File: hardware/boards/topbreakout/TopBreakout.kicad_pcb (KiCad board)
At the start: 2 copper layers, 75.6 x 73 mm, 46 parts, among them J1 WURTH_ELECTRONICS_61400413321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, J2 MOLEX_52892-3033MOLEX_52892-3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, J3 USB-A-S-X-X-VT, U1 ANALOG_DEVICES_AD7606BSTZANAL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, U3 ANALOG_DEVICES_AD5754BREZANAL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, U5 MICROCHIP_MCP1700T-2502E-TTMI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

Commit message: cleanup
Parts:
- removed MIDI_IN, MIDI_OUT: OG-MIDI_MAB5SHCUI-SD-50BV, OG-MIDI_SD-50BV
- added MIDI_IN1: OG-MIDI_MAB5SHCUI-SD-50BV, topbreakout:OG-MIDI_SD-50BV, F.Cu at (117.7, 91.4)
- added MIDI_OUT1: OG-MIDI_MAB5SHCUI-SD-50BV, topbreakout:OG-MIDI_SD-50BV, F.Cu at (178.7, 91.3)
- C1, C2, C3, C4: footprint C0805K -> topbreakout:C0805K
- C10, C11, C6, C9: footprint C1206 -> topbreakout:C1206
- C5, C7, C8: footprint 1206 -> topbreakout:1206
- J1: footprint WURTH_ELECTRONICS_61400413321_0 -> topbreakout:WURTH_ELECTRONICS_61400413321_0
- J2: value MOLEX_52892-3033MOLEX_52892-3033_0_0 -> MOLEX_52892-3033; footprint MOLEX_52892-3033_0 -> topbreakout:MOLEX_52892-3033_0
- J3: footprint USB-A-S-X-X-VT -> topbreakout:USB-A-S-X-X-VT
- J4: value (none) -> ST7735_1.4; footprint ST7735 -> topbreakout:ST7735
- JAD1, JAD2, JAD3, JAD4, JAD5, JAD6, JAD7, JAD8, JDA1, JDA2, JDA3, JDA4, JDA5, JDA6, JDA7, JDA8: footprint WQP-PJ301M-12_JACK -> topbreakout:WQP-PJ301M-12_JACK
- R10, R4, R7, R8, R9: footprint R0805 -> Capacitors_SMD:C_0805
- R11: footprint R0805 -> topbreakout:R0805
- TP1, TP3: footprint PAD.03X.05 -> topbreakout:PAD.03X.05
- U$1: footprint YAMAICHI_MICROSD_VERTICAL -> topbreakout:YAMAICHI_MICROSD_VERTICAL
- U$2: footprint TE_1-1734592-8 -> topbreakout:TE_1-1734592-8
- U1: footprint ANALOG_DEVICES_AD7606BSTZ_2 -> topbreakout:ANALOG_DEVICES_AD7606BSTZ_2
- U3: footprint ANALOG_DEVICES_AD5754BREZ_2 -> topbreakout:ANALOG_DEVICES_AD5754BREZ_2
- U5: value MICROCHIP_MCP1700T-2502E-TTMICROCHIP_MCP1700T-2502E-TT_0_0 -> MCP1700T-2502E; footprint MICROCHIP_MCP1700T-2502E-TT_0 -> topbreakout:MICROCHIP_MCP1700T-2502E-TT_0
- moved U5 27.1 mm to (117.3, 114.3), turned to 180 degrees
- moved C9 15.0 mm to (122.7, 114.3), turned to 0 degrees
- moved C6 14.9 mm to (128.8, 114.3), turned to 180 degrees
- moved C10 12.8 mm to (140.7, 138.3), turned to 270 degrees
- moved TP1 9.25 mm to (166.9, 136.4)
- moved R10 7.66 mm to (162.1, 139.8), turned to 180 degrees
- moved R4 6.29 mm to (157.6, 139.1), turned to 180 degrees
- moved C11 6.02 mm to (144.3, 138.3)
- moved U3 5.94 mm to (123.8, 121.9), turned to 0 degrees
- moved R9 5.33 mm to (153.3, 140.0), turned to 0 degrees
- moved TP3 5.31 mm to (119.1, 116.8)
- moved R8 4.04 mm to (148.7, 140.0), turned to 180 degrees
- moved C2 3.86 mm to (169.8, 136.4)
- moved C1 3.86 mm to (169.8, 133.9)
- moved C3 3.86 mm to (169.8, 131.4)
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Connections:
- net AD_AGND renamed /io_breakout-ver2.1_5/AD_AGND
- net AD_BYTE_SELECT renamed /io_breakout-ver2.1_5/AD_BYTE_SELECT
- net AD_OS0 renamed /io_breakout-ver2.1_5/AD_OS0
- net AD_RANGE renamed /io_breakout-ver2.1_5/AD_RANGE
- net AD_REFCAP_A renamed /io_breakout-ver2.1_5/AD_REFCAP_A
- net AD_REFSEL renamed /io_breakout-ver2.1_5/AD_REFSEL
- net AD_REGCAP1 renamed /io_breakout-ver2.1_5/AD_REGCAP1
- net AD_REGCAP2 renamed /io_breakout-ver2.1_5/AD_REGCAP2
- net AD_STBY renamed /io_breakout-ver2.1_5/AD_STBY
- net AGND renamed /io_breakout-ver2.1_5/AGND
- net AVIN renamed /io_breakout-ver2.1_5/AVIN
- net SD_CLK renamed /io_breakout-ver2.1_3/SD_CLK
- net SD_CS renamed /io_breakout-ver2.1_3/SD_CS
- net SD_DAT1 renamed /io_breakout-ver2.1_3/SD_DAT1
- net SD_DAT2 renamed /io_breakout-ver2.1_3/SD_DAT2
- net SD_DATAIN renamed /io_breakout-ver2.1_3/SD_DATAIN
- net SD_DATAOUT renamed /io_breakout-ver2.1_3/SD_DATAOUT
- net SD_GND renamed /io_breakout-ver2.1_3/SD_GND
- net SD_VCC renamed /io_breakout-ver2.1_3/SD_VCC
- net USB_A_D+ renamed /io_breakout-ver2.1_3/USB_A_D+
- net USB_A_D- renamed /io_breakout-ver2.1_3/USB_A_D-
- net USB_A_VCC renamed /io_breakout-ver2.1_3/USB_A_VCC
- net USB_B_D+ renamed /io_breakout-ver2.1_3/USB_B_D+
- net USB_B_D- renamed /io_breakout-ver2.1_3/USB_B_D-
- net USB_B_VCC renamed /io_breakout-ver2.1_3/USB_B_VCC
- net VREF renamed /io_breakout-ver2.1_6/VREF
- J2 pad 10: (no net) -> AVSS
- J2 pad 12: (no net) -> AVDD
- J2 pad 13: (no net) -> AVDD
- J2 pad 15: MIDI_IN_PIN5 -> /io_breakout-ver2.1_3/MIDI_IN_PIN5
- J2 pad 16: MIDI_IN_PIN4 -> /io_breakout-ver2.1_3/MIDI_IN_PIN4
- J2 pad 17: MIDI_OUT_PIN5 -> /io_breakout-ver2.1_3/MIDI_OUT_PIN5
- J2 pad 18: MIDI_OUT_PIN4 -> /io_breakout-ver2.1_3/MIDI_OUT_PIN4
- J2 pad 8: N$6 -> (no net)
- J2 pad 9: (no net) -> AVSS
- JDA5 pad P$1_TIP: DA_V5 -> (no net)
- JDA6 pad P$1_TIP: DA_V6 -> (no net)
- U1 pad 42: AD_REFINOUT -> (no net)
- U1 pad 57: AD_V5 -> (no net)
- U1 pad 59: AD_V6 -> (no net)
- U1 pad 61: AD_V7 -> (no net)
- U1 pad 63: AD_V8 -> (no net)
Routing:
- net /io_breakout-ver2.1_3/MIDI_OUT_PIN4: track 0.00 -> 84.7 mm, vias 0 -> 1
- net /io_breakout-ver2.1_3/MIDI_OUT_PIN5: track 0.00 -> 80.1 mm, vias 0 -> 1
- net MIDI_OUT_PIN4: track 75.0 -> 0.00 mm, vias 1 -> 0
- net MIDI_OUT_PIN5: track 74.2 -> 0.00 mm, vias 1 -> 0
- net /io_breakout-ver2.1_3/MIDI_IN_PIN4: track 0.00 -> 62.2 mm, vias 0 -> 1
- net MIDI_IN_PIN5: track 57.2 -> 0.00 mm
- net /io_breakout-ver2.1_3/MIDI_IN_PIN5: track 0.00 -> 48.2 mm, vias 0 -> 1
- net SPI0_MISO: track 89.0 -> 41.8 mm, vias 0 -> 3
- net MIDI_IN_PIN4: track 47.0 -> 0.00 mm
- net GND: track 5.42 -> 50.9 mm, vias 2 -> 45
- net /io_breakout-ver2.1_5/AD_AGND: track 81.3 -> 48.7 mm, vias 2 -> 1
- net /io_breakout-ver2.1_3/USB_B_D+: track 60.0 -> 91.1 mm, vias 1 -> 2
- net VIN: track 73.3 -> 102.7 mm
- net AVSS: track 0.00 -> 17.9 mm, vias 0 -> 2
- net /io_breakout-ver2.1_5/AD_REFSEL: track 11.5 -> 27.4 mm
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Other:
- rule trace_min: 0.2 -> 0.12
- rule via_min_drill: 0.3 -> 0.25

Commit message: minor
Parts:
- added J5: Conn_01x40, Connectors_TE-Connectivity:TE_2-84953-7_1x27_P1.0mm_Horizontal, F.Cu at (226.8, 98.8)
- J2: value MOLEX_52892-3033 -> MOLEX_52892-3033MOLEX_52892-3033_0_0
- R10, R4, R7, R8, R9: footprint Capacitors_SMD:C_0805 -> Resistors_SMD:R_0805
- R11: footprint topbreakout:R0805 -> Oddities:NetTie-I_Connected_SMD
- U5: value MCP1700T-2502E -> MICROCHIP_MCP1700T-2502E-TTMICROCHIP_MCP1700T-2502E-TT_0_0
- moved R4 1.69 mm to (157.2, 140.7), turned to 90 degrees
- moved R10 1.02 mm to (161.5, 140.7), turned to 90 degrees
- moved R9 1.01 mm to (153.9, 140.7), turned to 270 degrees
- moved R8 0.77 mm to (148.6, 140.7), turned to 90 degrees
- moved R11 0.17 mm to (155.8, 128.7), turned to 90 degrees
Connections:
- net /io_breakout-ver2.1_3/MIDI_IN_PIN4 renamed /FPC connector/MIDI_IN_PIN4
- net /io_breakout-ver2.1_3/MIDI_IN_PIN5 renamed /FPC connector/MIDI_IN_PIN5
- net /io_breakout-ver2.1_3/MIDI_OUT_PIN4 renamed /FPC connector/MIDI_OUT_PIN4
- net /io_breakout-ver2.1_3/MIDI_OUT_PIN5 renamed /FPC connector/MIDI_OUT_PIN5
- net /io_breakout-ver2.1_3/SD_CLK renamed /FPC connector/SD_CLK
- net /io_breakout-ver2.1_3/SD_CS renamed /FPC connector/SD_CS
- net /io_breakout-ver2.1_3/SD_DAT1 renamed /FPC connector/SD_DAT1
- net /io_breakout-ver2.1_3/SD_DAT2 renamed /FPC connector/SD_DAT2
- net /io_breakout-ver2.1_3/SD_DATAIN renamed /FPC connector/SD_DATAIN
- net /io_breakout-ver2.1_3/SD_DATAOUT renamed /FPC connector/SD_DATAOUT
- net /io_breakout-ver2.1_3/SD_GND renamed /FPC connector/SD_GND
- net /io_breakout-ver2.1_3/SD_VCC renamed /FPC connector/SD_VCC
- net /io_breakout-ver2.1_3/USB_A_D+ renamed /FPC connector/USB_A_D+
- net /io_breakout-ver2.1_3/USB_A_D- renamed /FPC connector/USB_A_D-
- net /io_breakout-ver2.1_3/USB_A_VCC renamed /FPC connector/USB_A_VCC
- net /io_breakout-ver2.1_3/USB_B_D+ renamed /FPC connector/USB_B_D+
- net /io_breakout-ver2.1_3/USB_B_D- renamed /FPC connector/USB_B_D-
- net /io_breakout-ver2.1_3/USB_B_VCC renamed /FPC connector/USB_B_VCC
- net /io_breakout-ver2.1_5/AD_AGND renamed /AD7606/AD_AGND
- net /io_breakout-ver2.1_5/AD_BYTE_SELECT renamed /AD7606/AD_BYTE_SELECT
- net /io_breakout-ver2.1_5/AD_OS0 renamed /AD7606/AD_OS0
- net /io_breakout-ver2.1_5/AD_RANGE renamed /AD7606/AD_RANGE
- net /io_breakout-ver2.1_5/AD_REFCAP_A renamed /AD7606/AD_REFCAP_A
- net /io_breakout-ver2.1_5/AD_REFSEL renamed /AD7606/AD_REFSEL
- net /io_breakout-ver2.1_5/AD_REGCAP1 renamed /AD7606/AD_REGCAP1
- net /io_breakout-ver2.1_5/AD_REGCAP2 renamed /AD7606/AD_REGCAP2
- net /io_breakout-ver2.1_5/AD_STBY renamed /AD7606/AD_STBY
- net /io_breakout-ver2.1_5/AGND renamed /AD7606/AGND
- net /io_breakout-ver2.1_5/AVIN renamed /AD7606/AVIN
- net /io_breakout-ver2.1_6/VREF renamed /AD5754 DAC/VREF
- JAD5 pad P$2_SWITCH: TAGND -> Net-(JAD5-PadP$2_SWITCH)
- JAD5 pad P$3_SLEEVE: TAGND -> Net-(JAD5-PadP$2_SWITCH)
- JAD6 pad P$2_SWITCH: TAGND -> Net-(JAD6-PadP$2_SWITCH)
- JAD6 pad P$3_SLEEVE: TAGND -> Net-(JAD6-PadP$2_SWITCH)
- JDA5 pad P$3_SLEEVE: TAGND -> GND
- JDA6 pad P$3_SLEEVE: TAGND -> GND
- JDA7 pad P$3_SLEEVE: (no net) -> GND
- JDA8 pad P$3_SLEEVE: (no net) -> GND
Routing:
- net GND: track 50.9 -> 73.7 mm, vias 45 -> 46
- net /AD7606/AD_AGND: track 48.7 -> 54.8 mm, vias 1 -> 4
- net 3V3: track 107.5 -> 111.5 mm, vias 3 -> 4
- net /FPC connector/USB_B_VCC: track 86.5 -> 88.4 mm
- net /AD7606/AD_STBY: track 7.45 -> 6.39 mm
- net /AD7606/AD_RANGE: track 11.1 -> 10.3 mm
- net /AD7606/AD_BYTE_SELECT: track 4.83 -> 5.37 mm

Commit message: moved midi circuit to breakout board
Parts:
- removed J5: Conn_01x40, Connectors_TE-Connectivity:TE_2-84953-7_1x27_P1.0mm_Horizontal
- added D1: D, Diodes_SMD:D_0805, B.Cu at (129.8, 92.6)
- added R1: 220, Resistors_SMD:R_0805_HandSoldering, B.Cu at (129.8, 83.6)
- added R2: 220, Resistors_SMD:R_0805_HandSoldering, B.Cu at (130.0, 97.0)
- added R3: 220, Resistors_SMD:R_0805_HandSoldering, B.Cu at (162.8, 90.9)
- added R5: 220, Resistors_SMD:R_0805_HandSoldering, B.Cu at (129.8, 88.1)
- added U$3: OPTO_DARL_6N138S, Mainboard:8-SMD, B.Cu at (145.8, 91.2)
- moved R10 2.70 mm to (163.6, 138.9)
- moved R4 2.29 mm to (158.7, 138.9)
- moved R8 1.80 mm to (148.8, 138.9)
- moved R9 1.79 mm to (153.8, 138.9)
- moved C3 1.56 mm to (169.8, 129.8)
- moved TP1 1.44 mm to (165.9, 135.4)
- moved C1 1.04 mm to (169.8, 132.9)
- moved C2 0.52 mm to (169.8, 135.9)
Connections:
- net /FPC connector/MIDI_IN_PIN4 renamed MIDI_IN_PIN4
- net /FPC connector/MIDI_IN_PIN5 renamed MIDI_IN_PIN5
- net /FPC connector/MIDI_OUT_PIN4 renamed MIDI_OUT_PIN4
- net /FPC connector/MIDI_OUT_PIN5 renamed MIDI_OUT_PIN5
- JAD5 pad P$1_TIP: (no net) -> AD_V5
- JAD6 pad P$1_TIP: (no net) -> AD_V6
- JAD7 pad P$1_TIP: (no net) -> AD_V7
- JAD8 pad P$1_TIP: (no net) -> AD_V8
- U1 pad 57: (no net) -> AD_V5
- U1 pad 59: (no net) -> AD_V6
- U1 pad 61: (no net) -> AD_V7
- U1 pad 63: (no net) -> AD_V8
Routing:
- net 3V3: track 111.5 -> 0.00 mm, vias 4 -> 0
- net VIN: track 102.7 -> 0.00 mm, vias 1 -> 0
- net /FPC connector/USB_B_D+: track 91.1 -> 0.00 mm, vias 2 -> 0
- net /FPC connector/USB_B_VCC: track 88.4 -> 0.00 mm, vias 1 -> 0
- net MIDI_OUT_PIN4: track 84.7 -> 0.00 mm, vias 1 -> 0
- net MIDI_OUT_PIN5: track 80.1 -> 0.00 mm, vias 1 -> 0
- net GND: track 73.7 -> 0.00 mm, vias 46 -> 0
- net SPI0_SCK: track 70.9 -> 0.00 mm, vias 2 -> 0
- net /FPC connector/USB_B_D-: track 70.5 -> 0.00 mm, vias 1 -> 0
- net AD_V1: track 68.4 -> 0.00 mm, vias 1 -> 0
- net AD_V2: track 65.9 -> 0.00 mm
- net MIDI_IN_PIN4: track 62.2 -> 0.00 mm, vias 1 -> 0
- net AD_V3: track 60.8 -> 0.00 mm
- net AD_V4: track 58.2 -> 0.00 mm
- net /AD7606/AD_AGND: track 54.8 -> 0.00 mm, vias 4 -> 0
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
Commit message: refactor
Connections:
- J2 pad 10: AVSS -> AVDD
- J2 pad 11: (no net) -> AVDD
- J2 pad 12: AVDD -> GATE_4
- J2 pad 13: AVDD -> GATE_3
- J2 pad 14: (no net) -> GATE_2
- J2 pad 15: MIDI_IN_PIN5 -> GATE_1
- J2 pad 16: MIDI_IN_PIN4 -> (no net)
- J2 pad 17: MIDI_OUT_PIN5 -> MIDI_TX
- J2 pad 18: MIDI_OUT_PIN4 -> MIDI_RX
- J2 pad 8: (no net) -> AVSS
- JDA5 pad P$1_TIP: (no net) -> GATE_1
- JDA6 pad P$1_TIP: (no net) -> GATE_2
- JDA7 pad P$1_TIP: (no net) -> GATE_3
- JDA8 pad P$1_TIP: (no net) -> GATE_4
- R3 pad 2: (no net) -> MIDI_TX

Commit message: imporvements
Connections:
- JAD5 pad P$2_SWITCH: Net-(JAD5-PadP$2_SWITCH) -> GND
- JAD5 pad P$3_SLEEVE: Net-(JAD5-PadP$2_SWITCH) -> GND
- JAD6 pad P$2_SWITCH: Net-(JAD6-PadP$2_SWITCH) -> GND
- JAD6 pad P$3_SLEEVE: Net-(JAD6-PadP$2_SWITCH) -> GND
- JAD7 pad P$2_SWITCH: (no net) -> GND
- JAD7 pad P$3_SLEEVE: (no net) -> GND
- JAD8 pad P$2_SWITCH: (no net) -> GND
- JAD8 pad P$3_SLEEVE: (no net) -> GND

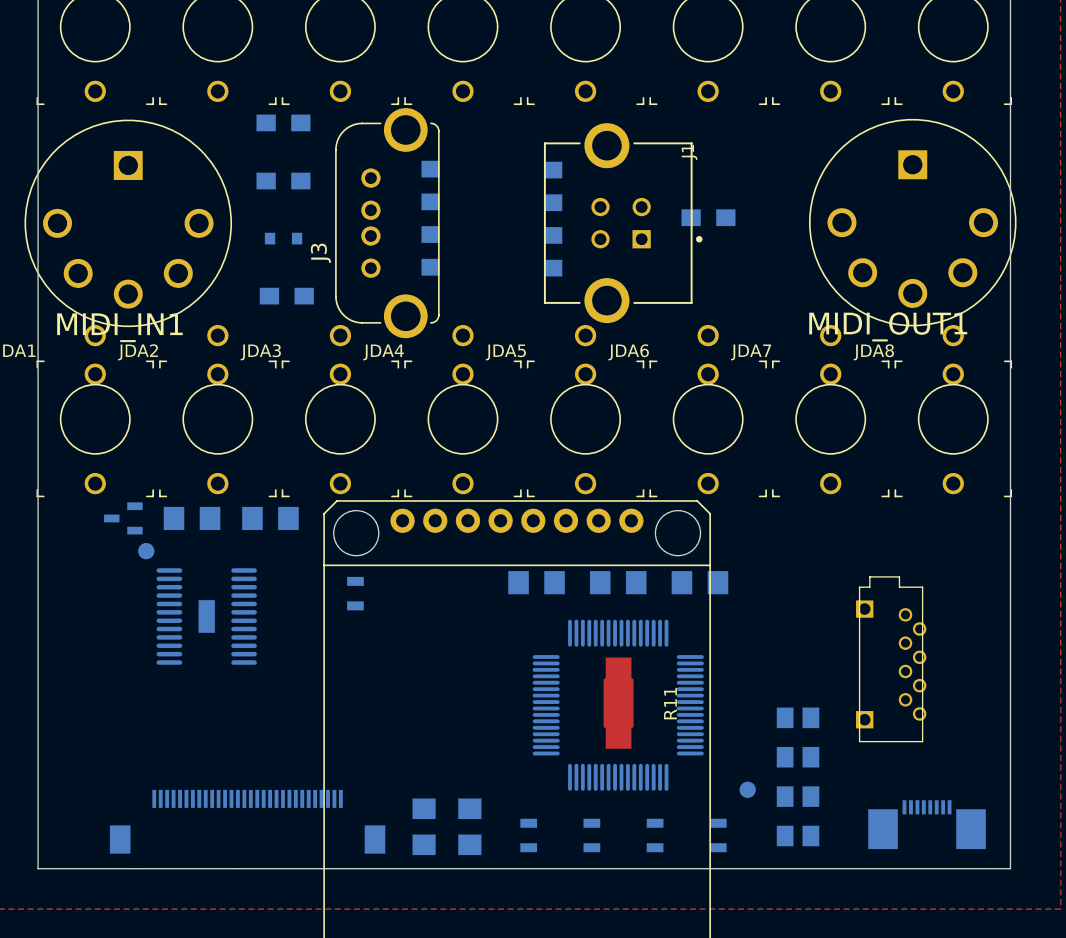
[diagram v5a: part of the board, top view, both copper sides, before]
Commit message: auto routed, not complete
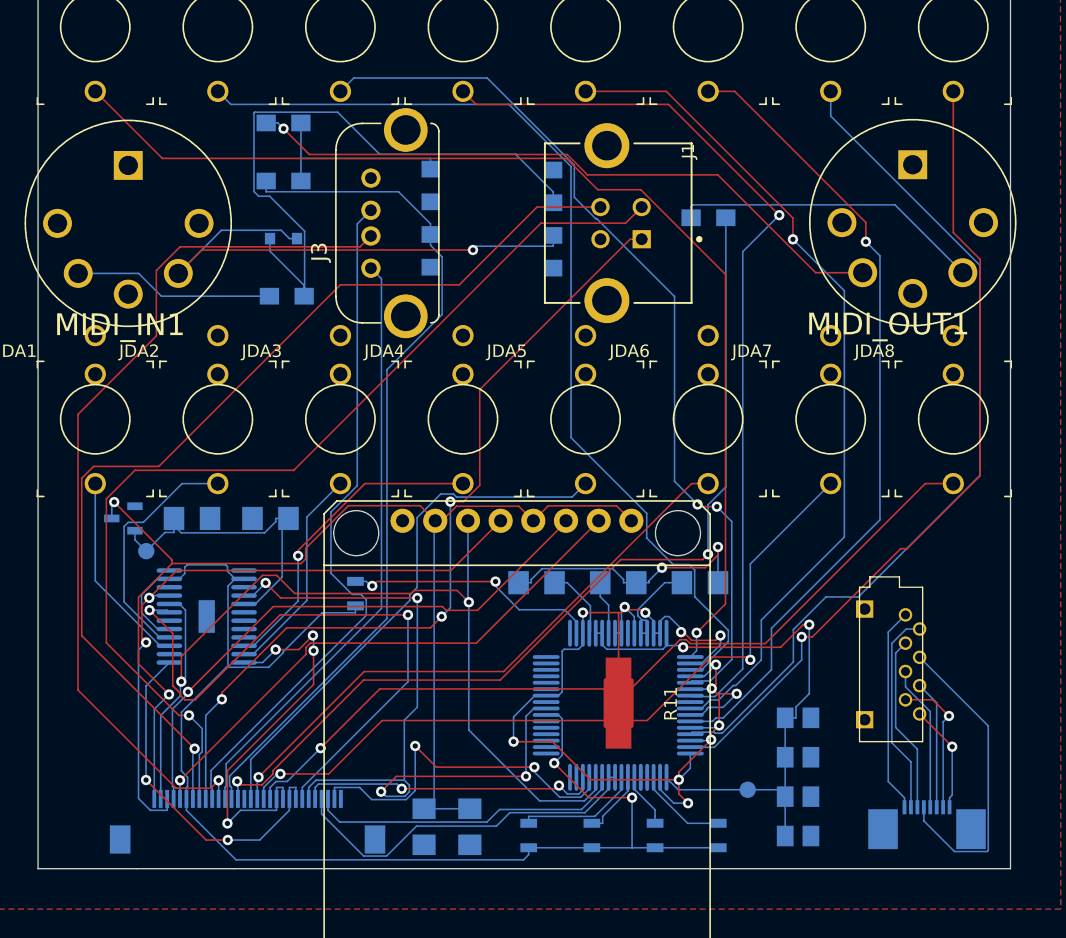
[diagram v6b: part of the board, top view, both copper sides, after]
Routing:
- net 3V3: track 0.00 -> 106.0 mm, vias 0 -> 2
- net VIN: track 0.00 -> 95.2 mm, vias 0 -> 2
- net /AD7606/AD_AGND: track 0.00 -> 88.2 mm, vias 0 -> 13
- net AD_V1: track 0.00 -> 85.7 mm, vias 0 -> 1
- net /FPC connector/USB_B_D-: track 0.00 -> 77.9 mm, vias 0 -> 1
- net /FPC connector/USB_B_D+: track 0.00 -> 77.6 mm, vias 0 -> 1
- net AD_V2: track 0.00 -> 76.5 mm
- net SPI0_SCK: track 0.00 -> 74.6 mm, vias 0 -> 2
- net MIDI_TX: track 0.00 -> 72.4 mm, vias 0 -> 2
- net AD_V4: track 0.00 -> 70.0 mm, vias 0 -> 1
- net AD_V3: track 0.00 -> 69.7 mm, vias 0 -> 2
- net /FPC connector/USB_A_D-: track 0.00 -> 68.7 mm, vias 0 -> 1
- net AD_V7: track 0.00 -> 67.0 mm
- net MIDI_RX: track 0.00 -> 66.6 mm
- net AD_V5: track 0.00 -> 65.9 mm, vias 0 -> 1
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
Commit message: routed, ERC checks success
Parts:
- C10, C11: footprint topbreakout:C1206 -> Capacitors_SMD:C_0805
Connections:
- C5 pad 2: /AD7606/AGND -> /AD7606/AD_AGND
- C7 pad 2: /AD7606/AGND -> /AD7606/AD_AGND
- C8 pad 2: /AD7606/AGND -> /AD7606/AD_AGND
- J2 pad 10: AVDD -> AVSS
- J2 pad 16: (no net) -> 3V3
- J2 pad 17: MIDI_TX -> VIN
- J2 pad 18: MIDI_RX -> GND
- J2 pad 25: 3V3 -> GND
- J2 pad 26: TFT_CS -> GND
- J2 pad 27: TFT_DC -> DA_SYNC
- J2 pad 29: SPI0_SCK -> MIDI_TX
- J2 pad 30: VIN -> MIDI_RX
- J2 pad 7: DA_SYNC -> SPI0_SCK
- J2 pad 8: AVSS -> TFT_CS
- J2 pad 9: AVSS -> TFT_DC
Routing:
- net GND: track 0.00 -> 76.1 mm, vias 0 -> 63
- net 3V3: track 106.0 -> 140.5 mm, vias 2 -> 4
- net GATE_3: track 59.3 -> 89.9 mm, vias 2 -> 0
- net DA_SYNC: track 47.5 -> 17.7 mm, vias 2 -> 0
- net /FPC connector/USB_A_D+: track 53.6 -> 80.1 mm
- net /AD7606/AGND: track 21.1 -> 0.00 mm, vias 2 -> 0
- net AVDD: track 31.0 -> 12.0 mm, vias 4 -> 2
- net Net-(D1-Pad1): track 48.0 -> 29.3 mm
- net /FPC connector/USB_B_D-: track 77.9 -> 60.2 mm, vias 1 -> 0
- net /FPC connector/USB_A_D-: track 68.7 -> 52.5 mm
- net /AD7606/AVIN: track 46.8 -> 63.0 mm, vias 2 -> 3
- net /FPC connector/USB_B_D+: track 77.6 -> 61.9 mm, vias 1 -> 0
- net /FPC connector/USB_A_VCC: track 46.6 -> 61.8 mm, vias 0 -> 1
- net AVSS: track 27.1 -> 14.3 mm
- net MIDI_TX: track 72.4 -> 84.9 mm, vias 2 -> 0
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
